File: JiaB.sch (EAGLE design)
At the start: 63 parts, among them J1 STEREO_JACK_SJ-3523, J2 STEREO_JACK_SJ-3523, J3 STEREO_JACK_SJ-3523, J4 STEREO_JACK_SJ-3523

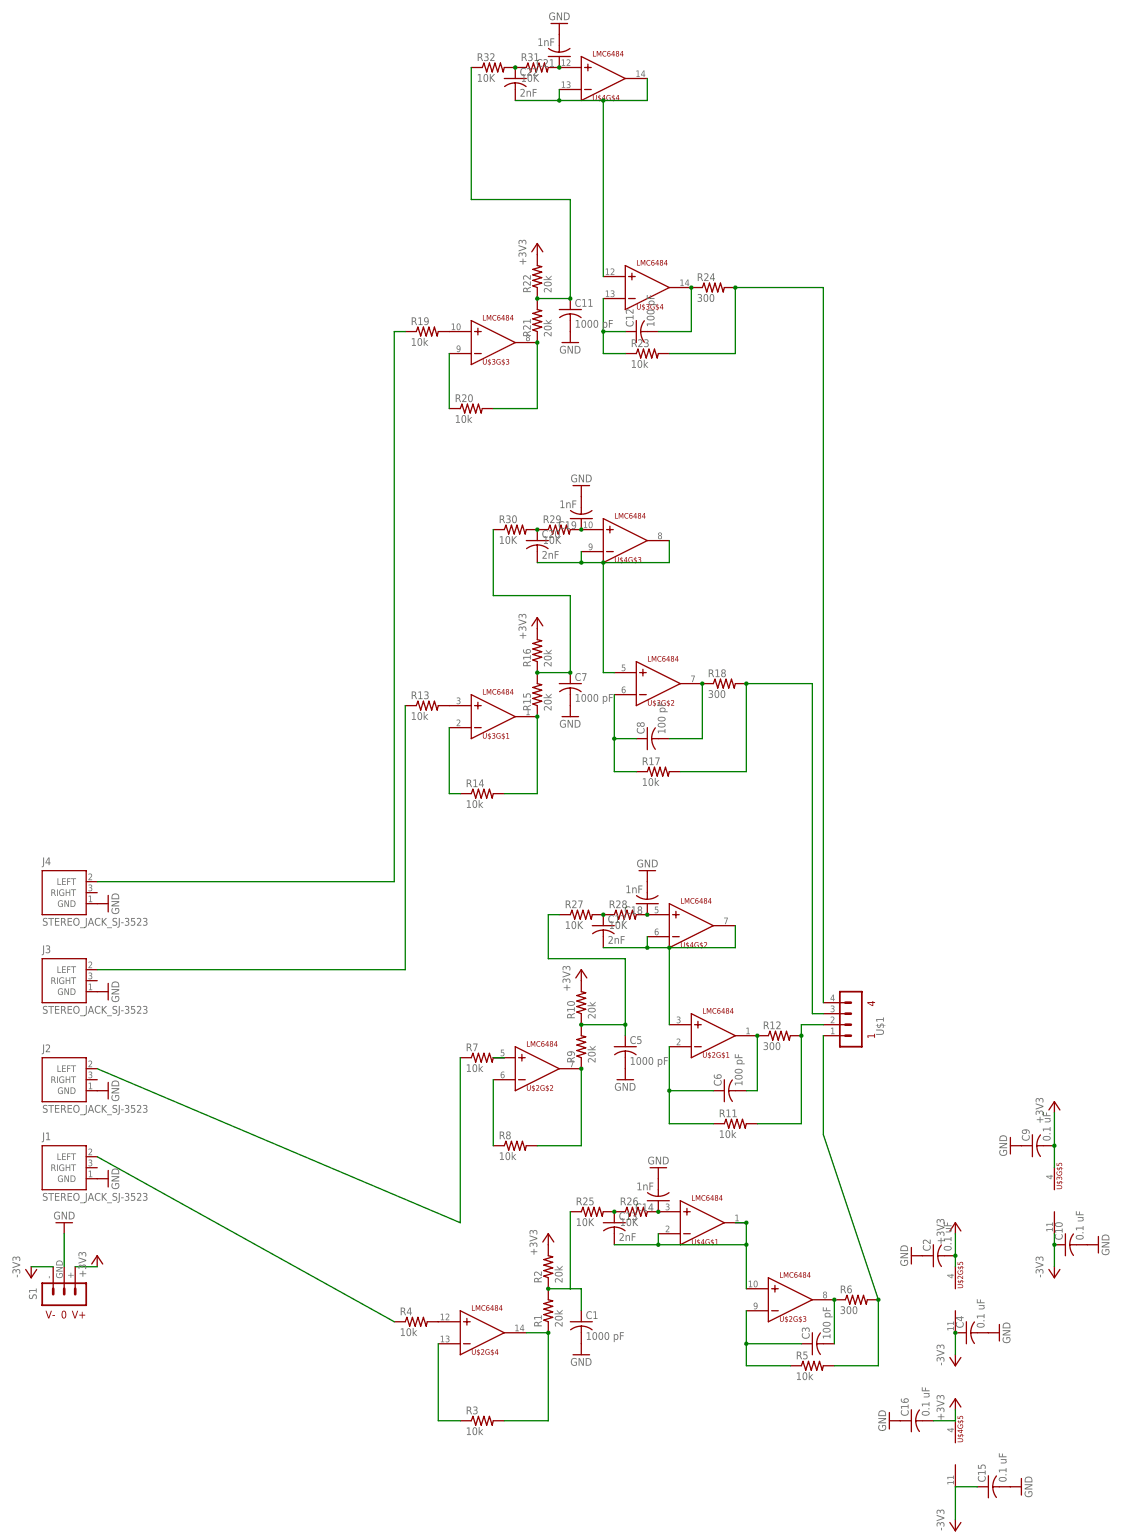
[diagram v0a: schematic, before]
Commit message: change anti-alias filter component values
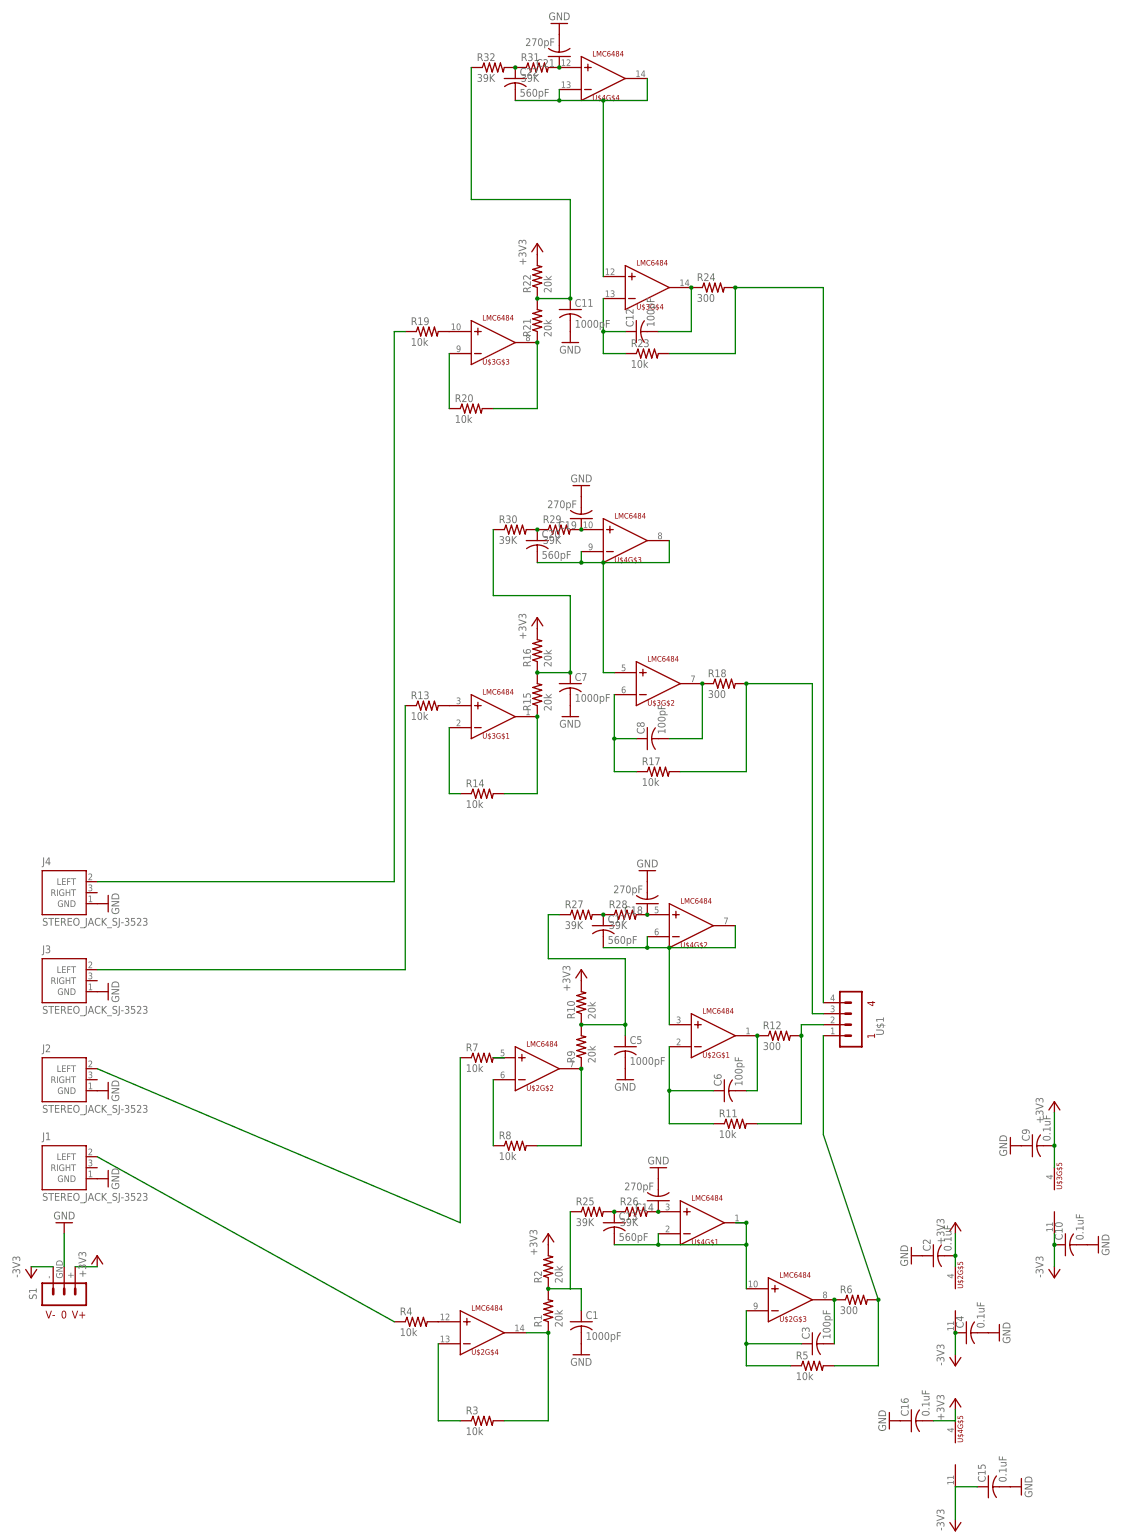
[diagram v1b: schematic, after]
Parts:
- C1, C11, C5, C7: value 1000 pF -> 1000pF
- C10, C15, C16, C2, C4, C9: value 0.1 uF -> 0.1uF
- C12, C3, C6, C8: value 100 pF -> 100pF
- C13, C17, C20, C22: value 2nF -> 560pF
- C14, C18, C19, C21: value 1nF -> 270pF
- R25, R26, R27, R28, R29, R30, R31, R32: value 10K -> 39K
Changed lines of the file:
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@@
 <?xml version="1.0" encoding="utf-8"?>
 <!DOCTYPE eagle SYSTEM "eagle.dtd">
-<eagle version="7.3.0">
+<eagle version="7.2.0">
 <drawing>
 <settings>
@@
 <part name="R5" library="resistor" deviceset="R-US_" device="0204/7" value="10k"/>
 <part name="R6" library="resistor" deviceset="R-US_" device="0204/7" value="300"/>
-<part name="C1" library="resistor" deviceset="C-US" device="025-025X050" value="1000 pF"/>
-<part name="C2" library="resistor" deviceset="C-US" device="025-025X050" value="0.1 uF"/>
-<part name="C3" library="resistor" deviceset="C-US" device="025-025X050" value="100 pF"/>
+<part name="C1" library="resistor" deviceset="C-US" device="025-025X050" value="1000pF"/>
+<part name="C2" library="resistor" deviceset="C-US" device="025-025X050" value="0.1uF"/>
+<part name="C3" library="resistor" deviceset="C-US" device="025-025X050" value="100pF"/>
 <part name="GND5" library="supply1" deviceset="GND" device=""/>
 <part name="GND7" library="supply1" deviceset="GND" device=""/>
 <part name="GND8" library="supply1" deviceset="GND" device=""/>
-<part name="C4" library="resistor" deviceset="C-US" device="025-025X050" value="0.1 uF"/>
+<part name="C4" library="resistor" deviceset="C-US" device="025-025X050" value="0.1uF"/>
 <part name="R7" library="resistor" deviceset="R-US_" device="0204/7" value="10k"/>
 <part name="R8" library="resistor" deviceset="R-US_" device="0204/7" value="10k"/>
@@
 <part name="R10" library="resistor" deviceset="R-US_" device="0204/7" value="20k"/>
 <part name="+3V4" library="RHD2000_eval_board" deviceset="+3V3" device=""/>
-<part name="C5" library="resistor" deviceset="C-US" device="025-025X050" value="1000 pF"/>
+<part name="C5" library="resistor" deviceset="C-US" device="025-025X050" value="1000pF"/>
 <part name="GND9" library="supply1" deviceset="GND" device=""/>
-<part name="C6" library="resistor" deviceset="C-US" device="025-025X050" value="100 pF"/>
+<part name="C6" library="resistor" deviceset="C-US" device="025-025X050" value="100pF"/>
 <part name="R11" library="resistor" deviceset="R-US_" device="0204/7" value="10k"/>
 <part name="R12" library="resistor" deviceset="R-US_" device="0204/7" value="300"/>
@@
 <part name="R16" library="resistor" deviceset="R-US_" device="0204/7" value="20k"/>
 <part name="+3V5" library="RHD2000_eval_board" deviceset="+3V3" device=""/>
-<part name="C7" library="resistor" deviceset="C-US" device="025-025X050" value="1000 pF"/>
+<part name="C7" library="resistor" deviceset="C-US" device="025-025X050" value="1000pF"/>
 <part name="GND10" library="supply1" deviceset="GND" device=""/>
-<part name="C8" library="resistor" deviceset="C-US" device="025-025X050" value="100 pF"/>
+<part name="C8" library="resistor" deviceset="C-US" device="025-025X050" value="100pF"/>
 <part name="R17" library="resistor" deviceset="R-US_" device="0204/7" value="10k"/>
 <part name="R18" library="resistor" deviceset="R-US_" device="0204/7" value="300"/>
-<part name="C9" library="resistor" deviceset="C-US" device="025-025X050" value="0.1 uF"/>
+<part name="C9" library="resistor" deviceset="C-US" device="025-025X050" value="0.1uF"/>
 <part name="GND11" library="supply1" deviceset="GND" device=""/>
 <part name="+3V6" library="RHD2000_eval_board" deviceset="+3V3" device=""/>
-<part name="C10" library="resistor" deviceset="C-US" device="025-025X050" value="0.1 uF"/>
+<part name="C10" library="resistor" deviceset="C-US" device="025-025X050" value="0.1uF"/>
 <part name="GND12" library="supply1" deviceset="GND" device=""/>
 <part name="-3V3" library="RHD2000_eval_board" deviceset="-3V3" device=""/>
@@
 <part name="R22" library="resistor" deviceset="R-US_" device="0204/7" value="20k"/>
 <part name="+3V7" library="RHD2000_eval_board" deviceset="+3V3" device=""/>
-<part name="C11" library="resistor" deviceset="C-US" device="025-025X050" value="1000 pF"/>
+<part name="C11" library="resistor" deviceset="C-US" device="025-025X050" value="1000pF"/>
 <part name="GND13" library="supply1" deviceset="GND" device=""/>
-<part name="C12" library="resistor" deviceset="C-US" device="025-025X050" value="100 pF"/>
+<part name="C12" library="resistor" deviceset="C-US" device="025-025X050" value="100pF"/>
 <part name="R23" library="resistor" deviceset="R-US_" device="0204/7" value="10k"/>
 <part name="R24" library="resistor" deviceset="R-US_" device="0204/7" value="300"/>
 <part name="U$4" library="kjbrown" deviceset="LMC6484" device=""/>
-<part name="R25" library="rcl" deviceset="R-US_" device="0204/7" value="10K"/>
-<part name="R26" library="rcl" deviceset="R-US_" device="0204/7" value="10K"/>
-<part name="C13" library="rcl" deviceset="C-US" device="025-025X050" value="2nF"/>
-<part name="C14" library="rcl" deviceset="C-US" device="025-025X050" value="1nF"/>
+<part name="R25" library="rcl" deviceset="R-US_" device="0204/7" value="39K"/>
+<part name="R26" library="rcl" deviceset="R-US_" device="0204/7" value="39K"/>
+<part name="C13" library="rcl" deviceset="C-US" device="025-025X050" value="560pF"/>
+<part name="C14" library="rcl" deviceset="C-US" device="025-025X050" value="270pF"/>
 <part name="GND14" library="supply1" deviceset="GND" device=""/>
 <part name="-3V4" library="RHD2000_eval_board" deviceset="-3V3" device=""/>
-<part name="C15" library="resistor" deviceset="C-US" device="025-025X050" value="0.1 uF"/>
+<part name="C15" library="resistor" deviceset="C-US" device="025-025X050" value="0.1uF"/>
 <part name="GND15" library="supply1" deviceset="GND" device=""/>
 <part name="+3V8" library="RHD2000_eval_board" deviceset="+3V3" device=""/>
-<part name="C16" library="resistor" deviceset="C-US" device="025-025X050" value="0.1 uF"/>
+<part name="C16" library="resistor" deviceset="C-US" device="025-025X050" value="0.1uF"/>
 <part name="GND16" library="supply1" deviceset="GND" device=""/>
-<part name="R27" library="rcl" deviceset="R-US_" device="0204/7" value="10K"/>
-<part name="R28" library="rcl" deviceset="R-US_" device="0204/7" value="10K"/>
-<part name="C17" library="rcl" deviceset="C-US" device="025-025X050" value="2nF"/>
-<part name="C18" library="rcl" deviceset="C-US" device="025-025X050" value="1nF"/>
+<part name="R27" library="rcl" deviceset="R-US_" device="0204/7" value="39K"/>
+<part name="R28" library="rcl" deviceset="R-US_" device="0204/7" value="39K"/>
+<part name="C17" library="rcl" deviceset="C-US" device="025-025X050" value="560pF"/>
+<part name="C18" library="rcl" deviceset="C-US" device="025-025X050" value="270pF"/>
 <part name="GND17" library="supply1" deviceset="GND" device=""/>
-<part name="R29" library="rcl" deviceset="R-US_" device="0204/7" value="10K"/>
-<part name="C19" library="rcl" deviceset="C-US" device="025-025X050" value="1nF"/>
+<part name="R29" library="rcl" deviceset="R-US_" device="0204/7" value="39K"/>
+<part name="C19" library="rcl" deviceset="C-US" device="025-025X050" value="270pF"/>
 <part name="GND18" library="supply1" deviceset="GND" device=""/>
-<part name="R30" library="rcl" deviceset="R-US_" device="0204/7" value="10K"/>
-<part name="C20" library="rcl" deviceset="C-US" device="025-025X050" value="2nF"/>
-<part name="C21" library="rcl" deviceset="C-US" device="025-025X050" value="1nF"/>
+<part name="R30" library="rcl" deviceset="R-US_" device="0204/7" value="39K"/>
+<part name="C20" library="rcl" deviceset="C-US" device="025-025X050" value="560pF"/>
+<part name="C21" library="rcl" deviceset="C-US" device="025-025X050" value="270pF"/>
 <part name="GND19" library="supply1" deviceset="GND" device=""/>
-<part name="R31" library="rcl" deviceset="R-US_" device="0204/7" value="10K"/>
-<part name="C22" library="rcl" deviceset="C-US" device="025-025X050" value="2nF"/>
-<part name="R32" library="rcl" deviceset="R-US_" device="0204/7" value="10K"/>
+<part name="R31" library="rcl" deviceset="R-US_" device="0204/7" value="39K"/>
+<part name="C22" library="rcl" deviceset="C-US" device="025-025X050" value="560pF"/>
+<part name="R32" library="rcl" deviceset="R-US_" device="0204/7" value="39K"/>
 </parts>
 <sheets>
